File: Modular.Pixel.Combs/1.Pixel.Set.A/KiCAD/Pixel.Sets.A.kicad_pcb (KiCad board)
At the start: 2 copper layers, 78 x 78 mm, 19 parts

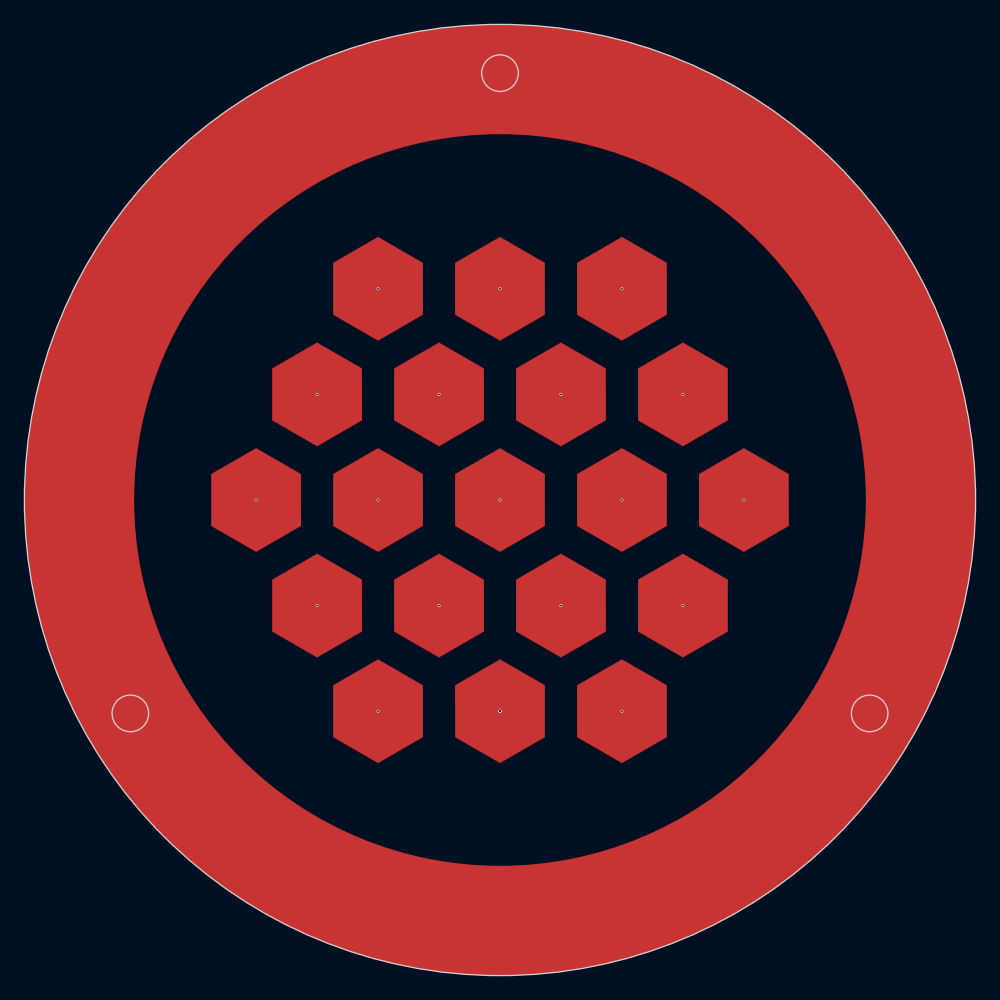
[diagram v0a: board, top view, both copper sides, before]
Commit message: Smoothed out Hexagon Pixels so that it Better Fits the Stencils
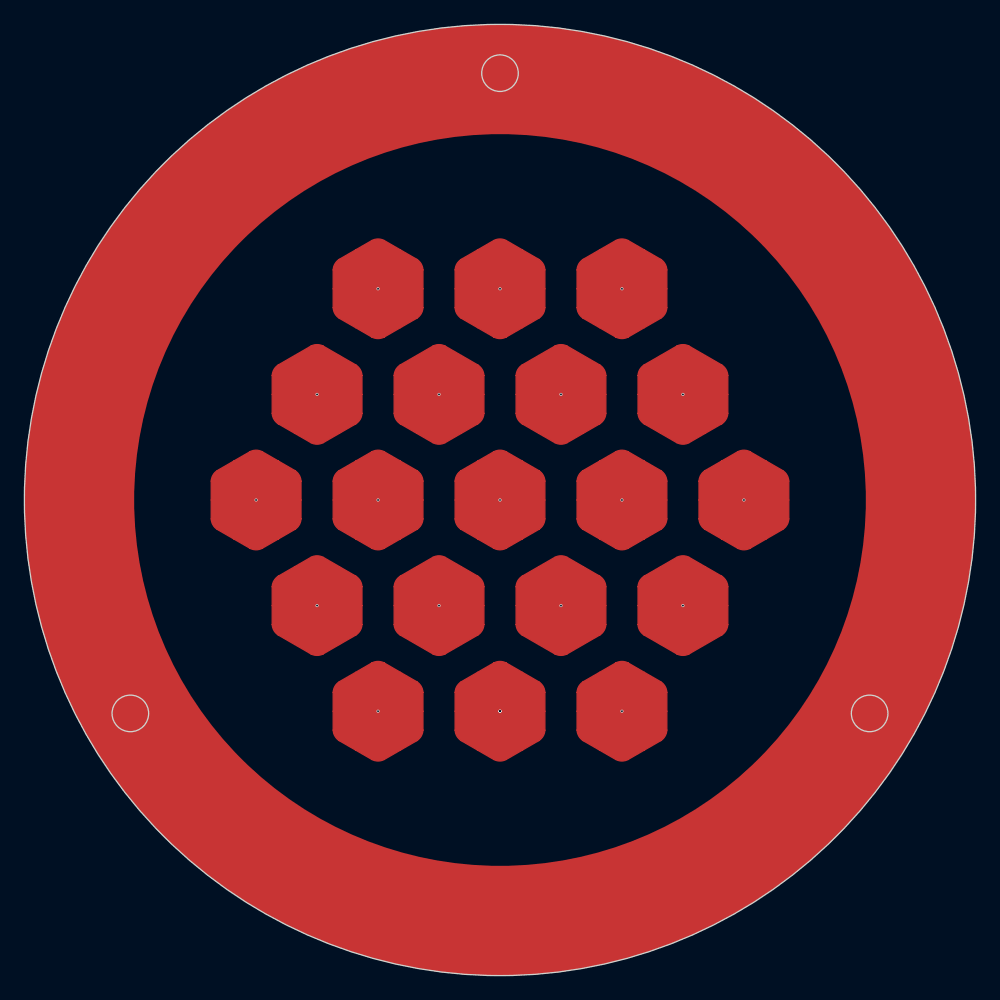
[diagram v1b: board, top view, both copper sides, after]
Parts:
- removed the REF** at (65.0, 58.3)
- removed REF**1, REF**19, REF**2, REF**20, REF**21, REF**23, REF**24, REF**25, REF**31, REF**32, REF**35, REF**36, REF**39, REF**4, REF**40, REF**49, REF**5, REF**8: Hex.Tile.Solid.Hex, Hex:Hex.Tile.Solid.Hex
- added REF**: Hex.Tile.Solid.Hex, 1.Hex:Hex.Tile.Solid.Hex, F.Cu at (65.0, 75.6)
- added REF**: Hex.Tile.Solid.Hex, 1.Hex:Hex.Tile.Solid.Hex, F.Cu at (55.0, 75.6)
- added REF**: Hex.Tile.Solid.Hex, 1.Hex:Hex.Tile.Solid.Hex, F.Cu at (60.0, 49.6)
- added REF**: Hex.Tile.Solid.Hex, 1.Hex:Hex.Tile.Solid.Hex, F.Cu at (85.0, 58.3)
- added REF**: Hex.Tile.Solid.Hex, 1.Hex:Hex.Tile.Solid.Hex, F.Cu at (80.0, 67.0)
- added REF**: Hex.Tile.Solid.Hex, 1.Hex:Hex.Tile.Solid.Hex, F.Cu at (55.0, 58.3)
- added REF**: Hex.Tile.Solid.Hex, 1.Hex:Hex.Tile.Solid.Hex, F.Cu at (50.0, 49.6)
- added REF**: Hex.Tile.Solid.Hex, 1.Hex:Hex.Tile.Solid.Hex, F.Cu at (75.0, 58.3)
- added REF**: Hex.Tile.Solid.Hex, 1.Hex:Hex.Tile.Solid.Hex, F.Cu at (65.0, 41.0)
- added REF**: Hex.Tile.Solid.Hex, 1.Hex:Hex.Tile.Solid.Hex, F.Cu at (50.0, 67.0)
- added REF**: Hex.Tile.Solid.Hex, 1.Hex:Hex.Tile.Solid.Hex, F.Cu at (60.0, 67.0)
- added REF**: Hex.Tile.Solid.Hex, 1.Hex:Hex.Tile.Solid.Hex, F.Cu at (75.0, 41.0)
- added REF**: Hex.Tile.Solid.Hex, 1.Hex:Hex.Tile.Solid.Hex, F.Cu at (75.0, 75.6)
- added REF**: Hex.Tile.Solid.Hex, 1.Hex:Hex.Tile.Solid.Hex, F.Cu at (55.0, 41.0)
- added REF**: Hex.Tile.Solid.Hex, 1.Hex:Hex.Tile.Solid.Hex, F.Cu at (80.0, 49.6)
- added REF**: Hex.Tile.Solid.Hex, 1.Hex:Hex.Tile.Solid.Hex, F.Cu at (45.0, 58.3)
- added REF**: Hex.Tile.Solid.Hex, 1.Hex:Hex.Tile.Solid.Hex, F.Cu at (70.0, 49.6)
- added REF**: Hex.Tile.Solid.Hex, 1.Hex:Hex.Tile.Solid.Hex, F.Cu at (65.0, 58.3)
- added REF**: Hex.Tile.Solid.Hex, 1.Hex:Hex.Tile.Solid.Hex, F.Cu at (70.0, 67.0)
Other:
- board text added: "Pixel Board A ::: May 2023 Alfredo Barajas Enriquez"
- board text removed: "Pixel Set A ::: May 2023 Alfredo Barajas Enriquez"

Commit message: Finalized Pixel Plane Design
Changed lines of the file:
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@@
     (fp_arc (start -1.549999 3.68) (mid -2.041539 3.53605) (end -2.411974 3.182339)
       (stroke (width 0.01) (type default)) (layer "F.Cu"))
-    (fp_arc (start 1.549999 -3.68) (mid 2.041539 -3.536049) (end 2.411974 -3.182339)
+    (fp_arc (start 1.549999 -3.68) (mid 2.04154 -3.53605) (end 2.411974 -3.182339)
       (stroke (width 0.01) (type default)) (layer "F.Cu"))
     (fp_arc (start 2.411974 3.182339) (mid 2.04154 3.536051) (end 1.549999 3.68)
@@
     (fp_arc (start -1.549999 3.68) (mid -2.041539 3.53605) (end -2.411974 3.182339)
       (stroke (width 0.01) (type default)) (layer "F.Cu"))
-    (fp_arc (start 1.549999 -3.68) (mid 2.041539 -3.536049) (end 2.411974 -3.182339)
+    (fp_arc (start 1.549999 -3.68) (mid 2.04154 -3.53605) (end 2.411974 -3.182339)
       (stroke (width 0.01) (type default)) (layer "F.Cu"))
     (fp_arc (start 2.411974 3.182339) (mid 2.04154 3.536051) (end 1.549999 3.68)
@@
     (fp_arc (start -1.549999 3.68) (mid -2.041539 3.53605) (end -2.411974 3.182339)
       (stroke (width 0.01) (type default)) (layer "F.Cu"))
-    (fp_arc (start 1.549999 -3.68) (mid 2.041539 -3.536049) (end 2.411974 -3.182339)
+    (fp_arc (start 1.549999 -3.68) (mid 2.04154 -3.53605) (end 2.411974 -3.182339)
       (stroke (width 0.01) (type default)) (layer "F.Cu"))
     (fp_arc (start 2.411974 3.182339) (mid 2.04154 3.536051) (end 1.549999 3.68)
@@
     (fp_arc (start -1.549999 3.68) (mid -2.041539 3.53605) (end -2.411974 3.182339)
       (stroke (width 0.01) (type default)) (layer "F.Cu"))
-    (fp_arc (start 1.549999 -3.68) (mid 2.041539 -3.536049) (end 2.411974 -3.182339)
+    (fp_arc (start 1.549999 -3.68) (mid 2.04154 -3.53605) (end 2.411974 -3.182339)
       (stroke (width 0.01) (type default)) (layer "F.Cu"))
     (fp_arc (start 2.411974 3.182339) (mid 2.04154 3.536051) (end 1.549999 3.68)
@@
     (fp_arc (start -1.549999 3.68) (mid -2.041539 3.53605) (end -2.411974 3.182339)
       (stroke (width 0.01) (type default)) (layer "F.Cu"))
-    (fp_arc (start 1.549999 -3.68) (mid 2.041539 -3.536049) (end 2.411974 -3.182339)
+    (fp_arc (start 1.549999 -3.68) (mid 2.04154 -3.53605) (end 2.411974 -3.182339)
       (stroke (width 0.01) (type default)) (layer "F.Cu"))
     (fp_arc (start 2.411974 3.182339) (mid 2.04154 3.536051) (end 1.549999 3.68)
@@
     (fp_arc (start -1.549999 3.68) (mid -2.041539 3.53605) (end -2.411974 3.182339)
       (stroke (width 0.01) (type default)) (layer "F.Cu"))
-    (fp_arc (start 1.549999 -3.68) (mid 2.041539 -3.536049) (end 2.411974 -3.182339)
+    (fp_arc (start 1.549999 -3.68) (mid 2.04154 -3.53605) (end 2.411974 -3.182339)
       (stroke (width 0.01) (type default)) (layer "F.Cu"))
     (fp_arc (start 2.411974 3.182339) (mid 2.04154 3.536051) (end 1.549999 3.68)
@@
     (fp_arc (start -1.549999 3.68) (mid -2.041539 3.53605) (end -2.411974 3.182339)
       (stroke (width 0.01) (type default)) (layer "F.Cu"))
-    (fp_arc (start 1.549999 -3.68) (mid 2.041539 -3.536049) (end 2.411974 -3.182339)
+    (fp_arc (start 1.549999 -3.68) (mid 2.04154 -3.53605) (end 2.411974 -3.182339)
       (stroke (width 0.01) (type default)) (layer "F.Cu"))
     (fp_arc (start 2.411974 3.182339) (mid 2.04154 3.536051) (end 1.549999 3.68)
@@
     (fp_arc (start -1.549999 3.68) (mid -2.041539 3.53605) (end -2.411974 3.182339)
       (stroke (width 0.01) (type default)) (layer "F.Cu"))
-    (fp_arc (start 1.549999 -3.68) (mid 2.041536 -3.536048) (end 2.411974 -3.182339)
+    (fp_arc (start 1.549999 -3.68) (mid 2.041539 -3.536049) (end 2.411974 -3.182339)
       (stroke (width 0.01) (type default)) (layer "F.Cu"))
     (fp_arc (start 2.411974 3.182339) (mid 2.04154 3.536051) (end 1.549999 3.68)
@@
     (fp_arc (start -1.549999 3.68) (mid -2.041539 3.53605) (end -2.411974 3.182339)
       (stroke (width 0.01) (type default)) (layer "F.Cu"))
-    (fp_arc (start 1.549999 -3.68) (mid 2.041539 -3.536049) (end 2.411974 -3.182339)
+    (fp_arc (start 1.549999 -3.68) (mid 2.04154 -3.53605) (end 2.411974 -3.182339)
       (stroke (width 0.01) (type default)) (layer "F.Cu"))
     (fp_arc (start 2.411974 3.182339) (mid 2.04154 3.536051) (end 1.549999 3.68)
@@
     (fp_arc (start -1.549999 3.68) (mid -2.041539 3.53605) (end -2.411974 3.182339)
       (stroke (width 0.01) (type default)) (layer "F.Cu"))
-    (fp_arc (start 1.549999 -3.68) (mid 2.041539 -3.536049) (end 2.411974 -3.182339)
+    (fp_arc (start 1.549999 -3.68) (mid 2.04154 -3.53605) (end 2.411974 -3.182339)
       (stroke (width 0.01) (type default)) (layer "F.Cu"))
     (fp_arc (start 2.411974 3.182339) (mid 2.04154 3.536051) (end 1.549999 3.68)
@@
     (fp_arc (start -1.549999 3.68) (mid -2.041539 3.53605) (end -2.411974 3.182339)
       (stroke (width 0.01) (type default)) (layer "F.Cu"))
-    (fp_arc (start 1.549999 -3.68) (mid 2.041539 -3.536049) (end 2.411974 -3.182339)
+    (fp_arc (start 1.549999 -3.68) (mid 2.04154 -3.53605) (end 2.411974 -3.182339)
       (stroke (width 0.01) (type default)) (layer "F.Cu"))
     (fp_arc (start 2.411974 3.182339) (mid 2.04154 3.536051) (end 1.549999 3.68)
@@
     (fp_arc (start -1.549999 3.68) (mid -2.041539 3.53605) (end -2.411974 3.182339)
       (stroke (width 0.01) (type default)) (layer "F.Cu"))
-    (fp_arc (start 1.549999 -3.68) (mid 2.041539 -3.536049) (end 2.411974 -3.182339)
+    (fp_arc (start 1.549999 -3.68) (mid 2.04154 -3.53605) (end 2.411974 -3.182339)
       (stroke (width 0.01) (type default)) (layer "F.Cu"))
     (fp_arc (start 2.411974 3.182339) (mid 2.04154 3.536051) (end 1.549999 3.68)
@@
     (fp_arc (start -1.549999 3.68) (mid -2.041539 3.53605) (end -2.411974 3.182339)
       (stroke (width 0.01) (type default)) (layer "F.Cu"))
-    (fp_arc (start 1.549999 -3.68) (mid 2.041539 -3.536049) (end 2.411974 -3.182339)
+    (fp_arc (start 1.549999 -3.68) (mid 2.04154 -3.53605) (end 2.411974 -3.182339)
       (stroke (width 0.01) (type default)) (layer "F.Cu"))
     (fp_arc (start 2.411974 3.182339) (mid 2.04154 3.536051) (end 1.549999 3.68)
@@
     (fp_arc (start -1.549999 3.68) (mid -2.041539 3.53605) (end -2.411974 3.182339)
       (stroke (width 0.01) (type default)) (layer "F.Cu"))
-    (fp_arc (start 1.549999 -3.68) (mid 2.041539 -3.536049) (end 2.411974 -3.182339)
+    (fp_arc (start 1.549999 -3.68) (mid 2.04154 -3.53605) (end 2.411974 -3.182339)
       (stroke (width 0.01) (type default)) (layer "F.Cu"))
     (fp_arc (start 2.411974 3.182339) (mid 2.04154 3.536051) (end 1.549999 3.68)
@@
     (fp_arc (start -1.549999 3.68) (mid -2.041539 3.53605) (end -2.411974 3.182339)
       (stroke (width 0.01) (type default)) (layer "F.Cu"))
-    (fp_arc (start 1.549999 -3.68) (mid 2.041539 -3.536049) (end 2.411974 -3.182339)
+    (fp_arc (start 1.549999 -3.68) (mid 2.04154 -3.53605) (end 2.411974 -3.182339)
       (stroke (width 0.01) (type default)) (layer "F.Cu"))
     (fp_arc (start 2.411974 3.182339) (mid 2.04154 3.536051) (end 1.549999 3.68)
@@
     (fp_arc (start -1.549999 3.68) (mid -2.041539 3.53605) (end -2.411974 3.182339)
       (stroke (width 0.01) (type default)) (layer "F.Cu"))
-    (fp_arc (start 1.549999 -3.68) (mid 2.041539 -3.536049) (end 2.411974 -3.182339)
+    (fp_arc (start 1.549999 -3.68) (mid 2.04154 -3.53605) (end 2.411974 -3.182339)
       (stroke (width 0.01) (type default)) (layer "F.Cu"))
     (fp_arc (start 2.411974 3.182339) (mid 2.04154 3.536051) (end 1.549999 3.68)
@@
     (fp_arc (start -1.549999 3.68) (mid -2.041539 3.53605) (end -2.411974 3.182339)
       (stroke (width 0.01) (type default)) (layer "F.Cu"))
-    (fp_arc (start 1.549999 -3.68) (mid 2.041539 -3.536049) (end 2.411974 -3.182339)
+    (fp_arc (start 1.549999 -3.68) (mid 2.04154 -3.53605) (end 2.411974 -3.182339)
       (stroke (width 0.01) (type default)) (layer "F.Cu"))
     (fp_arc (start 2.411974 3.182339) (mid 2.04154 3.536051) (end 1.549999 3.68)
@@
     (fp_arc (start -1.549999 3.68) (mid -2.041539 3.53605) (end -2.411974 3.182339)
       (stroke (width 0.01) (type default)) (layer "F.Cu"))
-    (fp_arc (start 1.549999 -3.68) (mid 2.041539 -3.536049) (end 2.411974 -3.182339)
+    (fp_arc (start 1.549999 -3.68) (mid 2.04154 -3.53605) (end 2.411974 -3.182339)
       (stroke (width 0.01) (type default)) (layer "F.Cu"))
     (fp_arc (start 2.411974 3.182339) (mid 2.04154 3.536051) (end 1.549999 3.68)
@@
     (fp_arc (start -1.549999 3.68) (mid -2.041539 3.53605) (end -2.411974 3.182339)
       (stroke (width 0.01) (type default)) (layer "F.Cu"))
-    (fp_arc (start 1.549999 -3.68) (mid 2.041539 -3.536049) (end 2.411974 -3.182339)
+    (fp_arc (start 1.549999 -3.68) (mid 2.04154 -3.53605) (end 2.411974 -3.182339)
       (stroke (width 0.01) (type default)) (layer "F.Cu"))
     (fp_arc (start 2.411974 3.182339) (mid 2.04154 3.536051) (end 1.549999 3.68)

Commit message: Minor Fixes
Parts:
- added G***: LOGO, LOGO, B.Cu at (74.6, 87.9)
